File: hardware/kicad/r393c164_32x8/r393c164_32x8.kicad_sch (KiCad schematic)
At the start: 65 parts, among them J1 Conn_01x05_Pin, Q1 NTS2101P, Q2 NTS2101P, Q3 NTS2101P, Q4 NTS2101P, Q5 NTS2101P, Q6 NTS2101P, Q7 NTS2101P, Q8 NTS2101P, U1 74LS393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

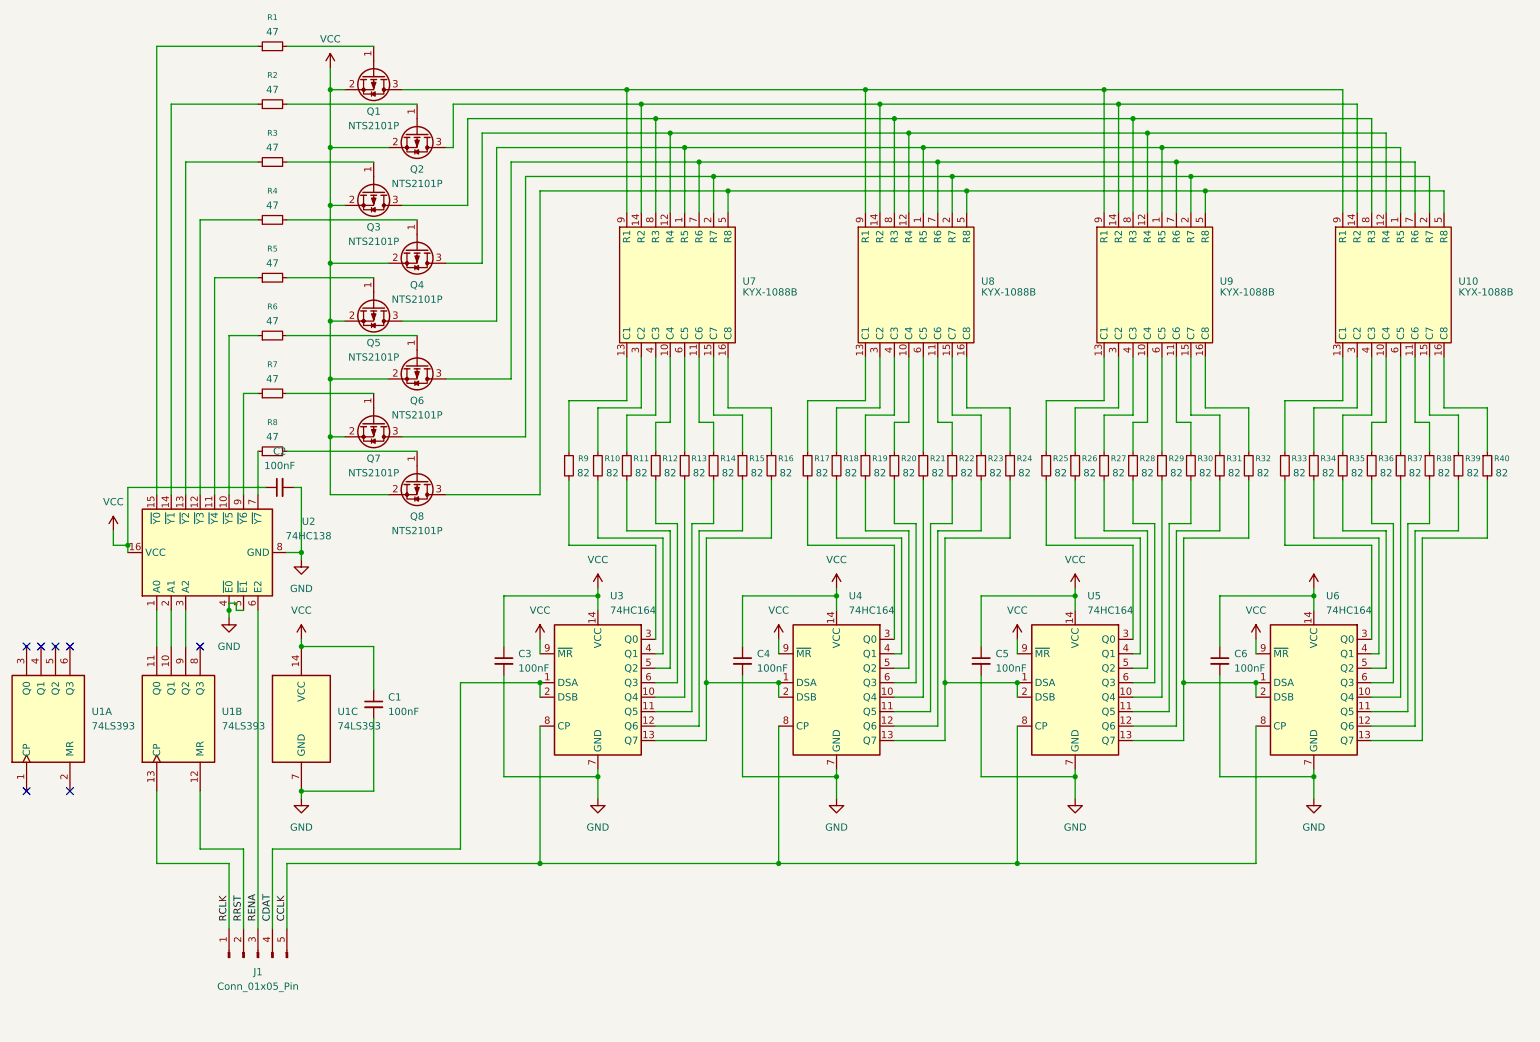
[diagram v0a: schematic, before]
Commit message: r393c164_32x8: Update KiCad schematic
* Renamed references `U3` -- `U10`
* Replaced P-channel MOSFET by `IRLML6401`
* Added VCC + GND connector (`J2`)
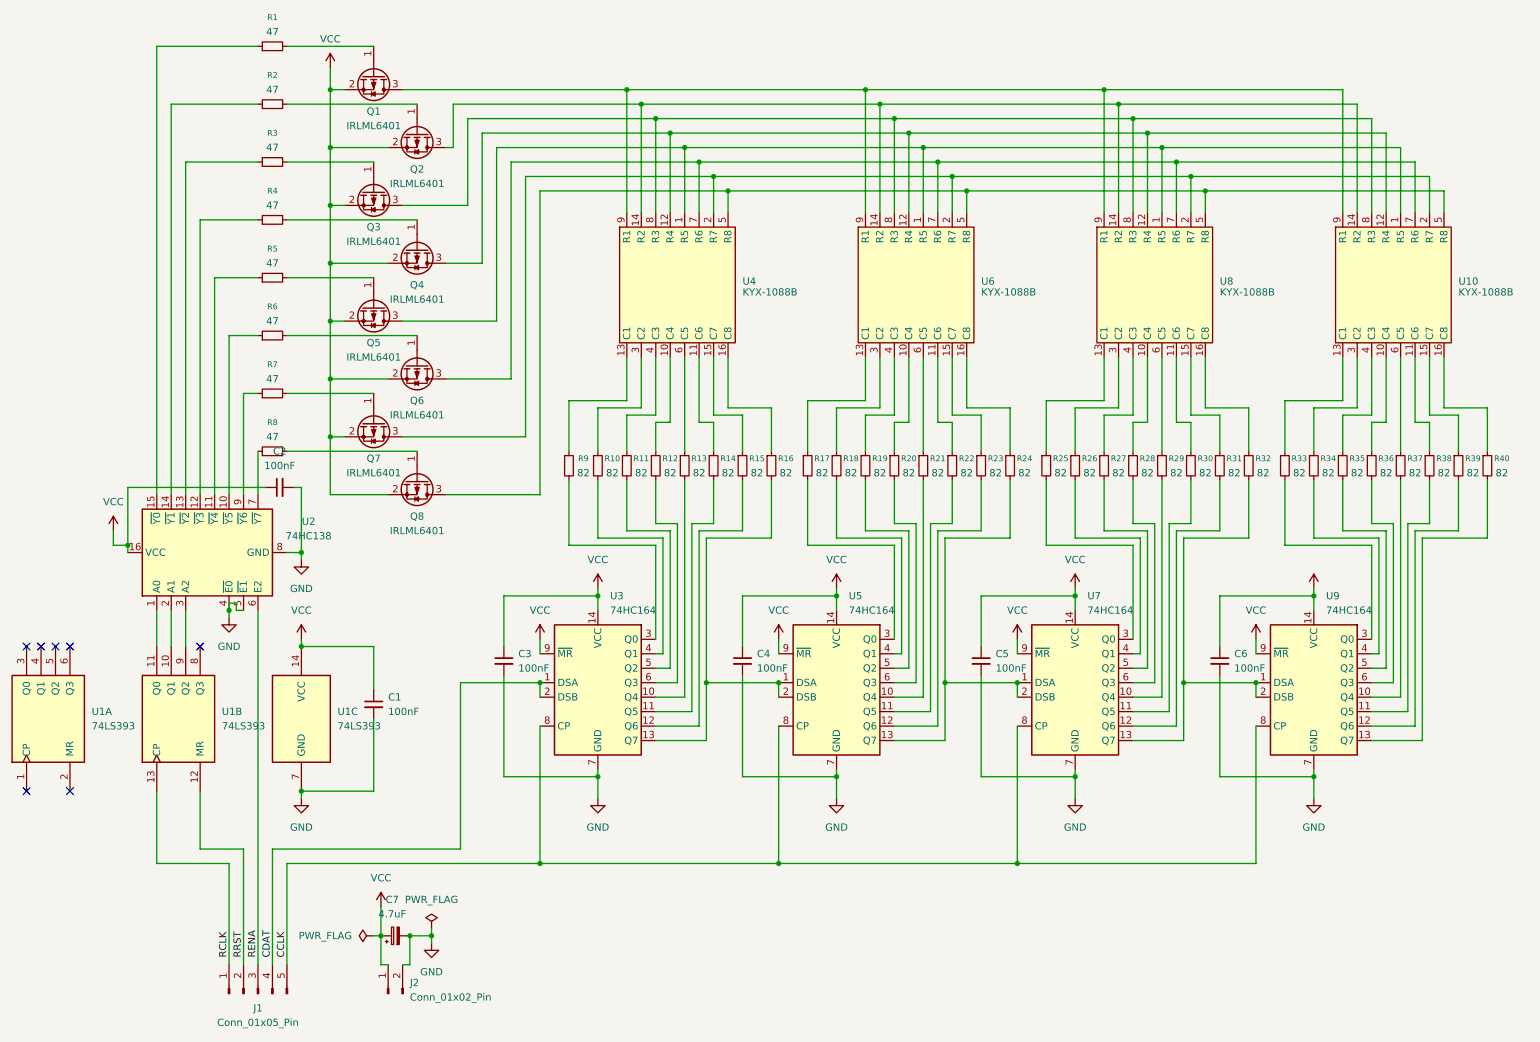
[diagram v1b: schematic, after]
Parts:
- added C7: 4.7uF, Capacitor_THT:CP_Radial_D4.0mm_P2.00mm, symbol Device:C_Polarized_Small
- added J2: Conn_01x02_Pin, Connector_PinHeader_2.54mm:PinHeader_1x02_P2.54mm_Vertical, symbol Connector:Conn_01x02_Pin
- Q1, Q2, Q3, Q4, Q5, Q6, Q7, Q8: value NTS2101P -> IRLML6401
- renumbered U7 to U4, U4 to U5, U8 to U6, U5 to U7, U9 to U8, U6 to U9
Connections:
- net GND: now also C7.2, J2.2 (Pin_2)
- net VCC: now also C7.1, J2.1 (Pin_1)
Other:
- moved on the sheet: J1

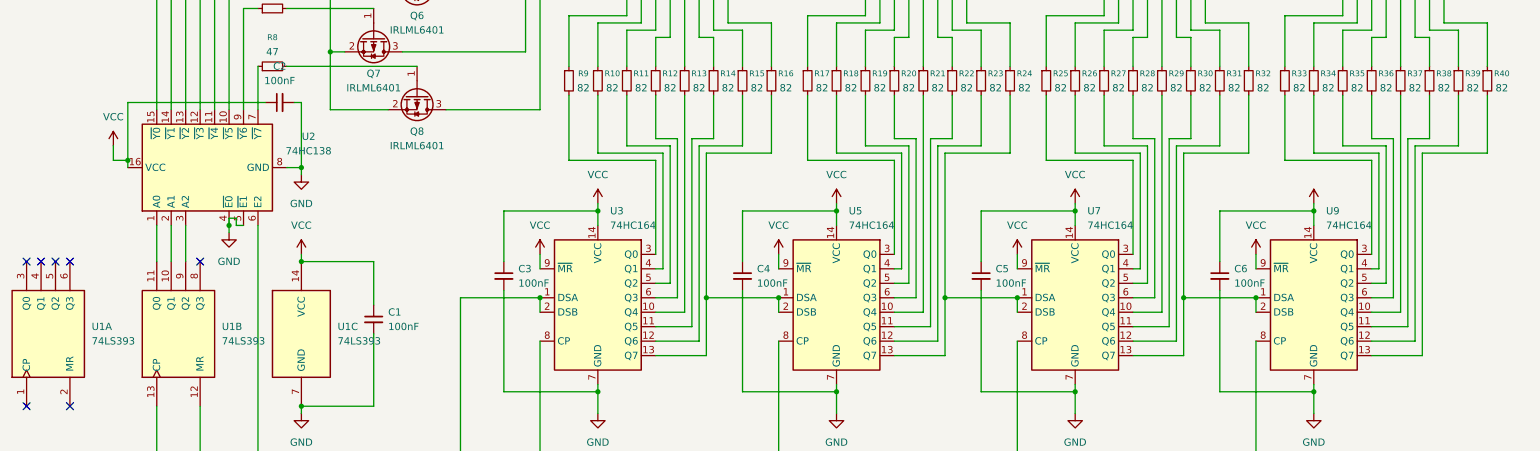
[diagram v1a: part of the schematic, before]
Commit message: r393c164_32x8: fix defects in KiCad schematic / PCB
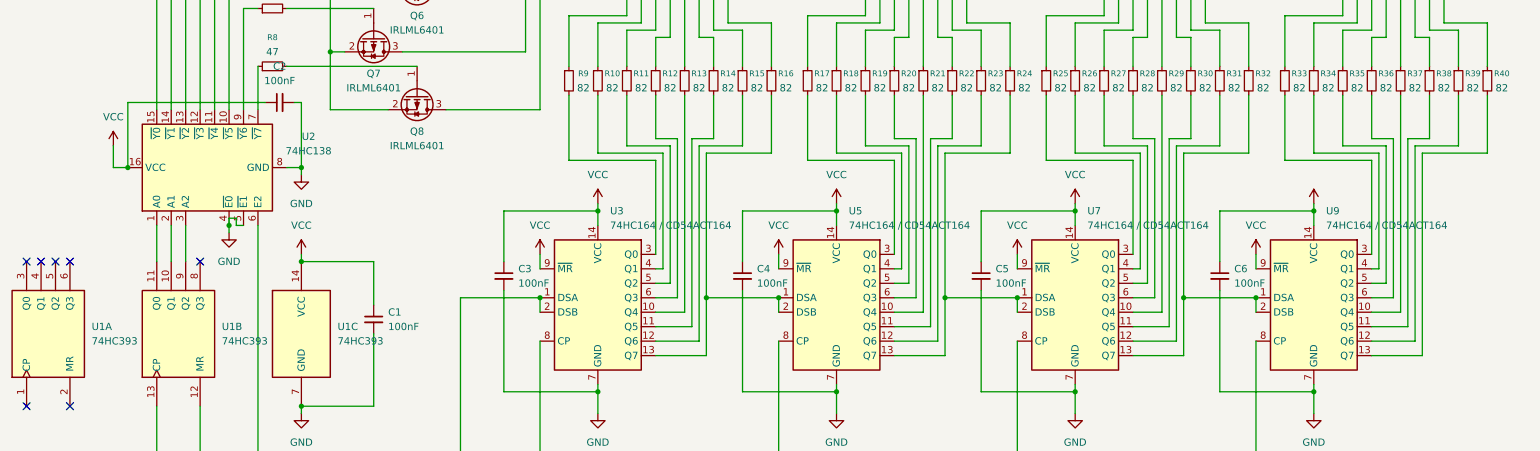
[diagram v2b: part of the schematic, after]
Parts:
- U1: value 74LS393 -> 74HC393
- U3, U5, U7, U9: value 74HC164 -> 74HC164 / CD54ACT164
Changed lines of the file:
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@@
 	)
 	(junction
+		(at 38.1 106.68)
+		(diameter 0)
+		(color 0 0 0 0)
+	)
+	(junction
 		(at 110.49 129.54)
 		(diameter 0)
@@
 	)
 	(junction
-		(at 38.1 105.41)
-		(diameter 0)
-		(color 0 0 0 0)
-	)
-	(junction
 		(at 120.65 114.3)
 		(diameter 0)
@@
 	(wire
 		(pts
-			(xy 35.56 102.87) (xy 35.56 105.41)
+			(xy 35.56 102.87) (xy 35.56 106.68)
 		)
 		(stroke
@@
 	(wire
 		(pts
+			(xy 38.1 95.25) (xy 38.1 106.68)
+		)
+		(stroke
+			(width 0)
+			(type default)
+		)
+	)
+	(wire
+		(pts
 			(xy 120.65 104.14) (xy 132.08 104.14)
 		)
@@
 	(wire
 		(pts
-			(xy 38.1 106.68) (xy 38.1 105.41)
-		)
-		(stroke
-			(width 0)
-			(type default)
-		)
-	)
-	(wire
-		(pts
 			(xy 66.04 27.94) (xy 88.9 27.94)
 		)
@@
 	(wire
 		(pts
-			(xy 35.56 105.41) (xy 38.1 105.41)
+			(xy 35.56 106.68) (xy 38.1 106.68)
 		)
 		(stroke
@@
 	(wire
 		(pts
-			(xy 38.1 95.25) (xy 38.1 105.41)
-		)
-		(stroke
-			(width 0)
-			(type default)
-		)
-	)
-	(wire
-		(pts
 			(xy 50.8 48.26) (xy 50.8 96.52)
 		)
@@
 			)
 		)
-		(property "Value" "74HC164"
+		(property "Value" "74HC164 / CD54ACT164"
 			(at 164.7033 116.84 0)
 			(effects
@@
 			)
 		)
-		(property "Value" "74HC164"
+		(property "Value" "74HC164 / CD54ACT164"
 			(at 122.7933 116.84 0)
 			(effects
@@
 			)
 		)
-		(property "Value" "74HC164"
+		(property "Value" "74HC164 / CD54ACT164"
 			(at 248.5233 116.84 0)
 			(effects
@@
 			)
 		)
-		(property "Value" "74LS393"
+		(property "Value" "74HC393"
 			(at 31.75 137.1599 90)
 			(effects
@@
 			)
 		)
-		(property "Value" "74LS393"
+		(property "Value" "74HC393"
 			(at 54.61 137.1599 90)
 			(effects
@@
 			)
 		)
-		(property "Value" "74HC164"
+		(property "Value" "74HC164 / CD54ACT164"
 			(at 206.6133 116.84 0)
 			(effects
@@
 			)
 		)
-		(property "Value" "74LS393"
+		(property "Value" "74HC393"
 			(at 74.93 137.1599 0)
 			(effects
